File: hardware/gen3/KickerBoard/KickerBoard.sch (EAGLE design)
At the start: 87 parts, among them IC1 TL331, Q3 MOSFET-NCHANNELFQP30N06L, Q4 MOSFET-NCHANNELBSS123LT1G, Q6 MOSFET-PCHANNEL, U1 NC7WZ08K8X, U2 ATMEGA165PV-8AU

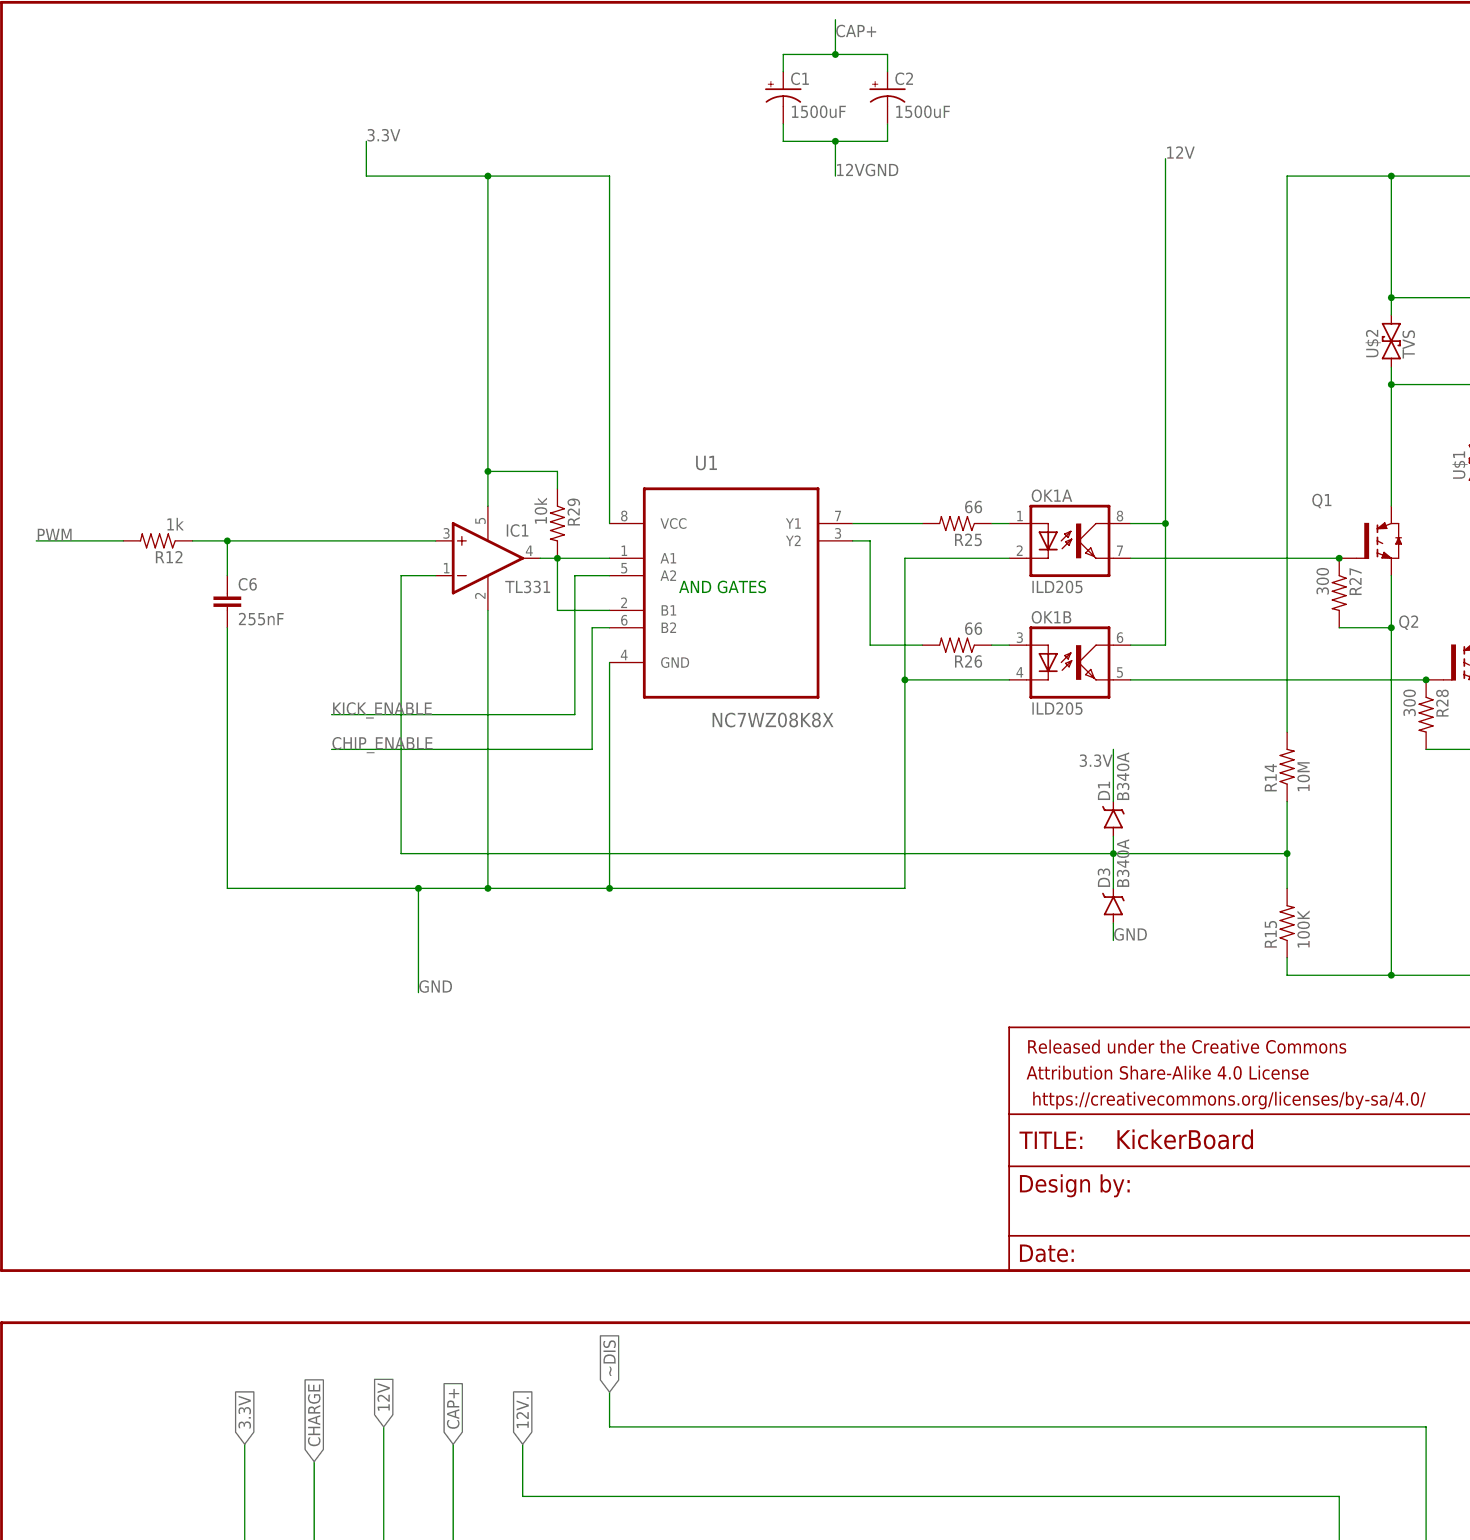
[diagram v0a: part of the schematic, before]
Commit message: reading in fault pins
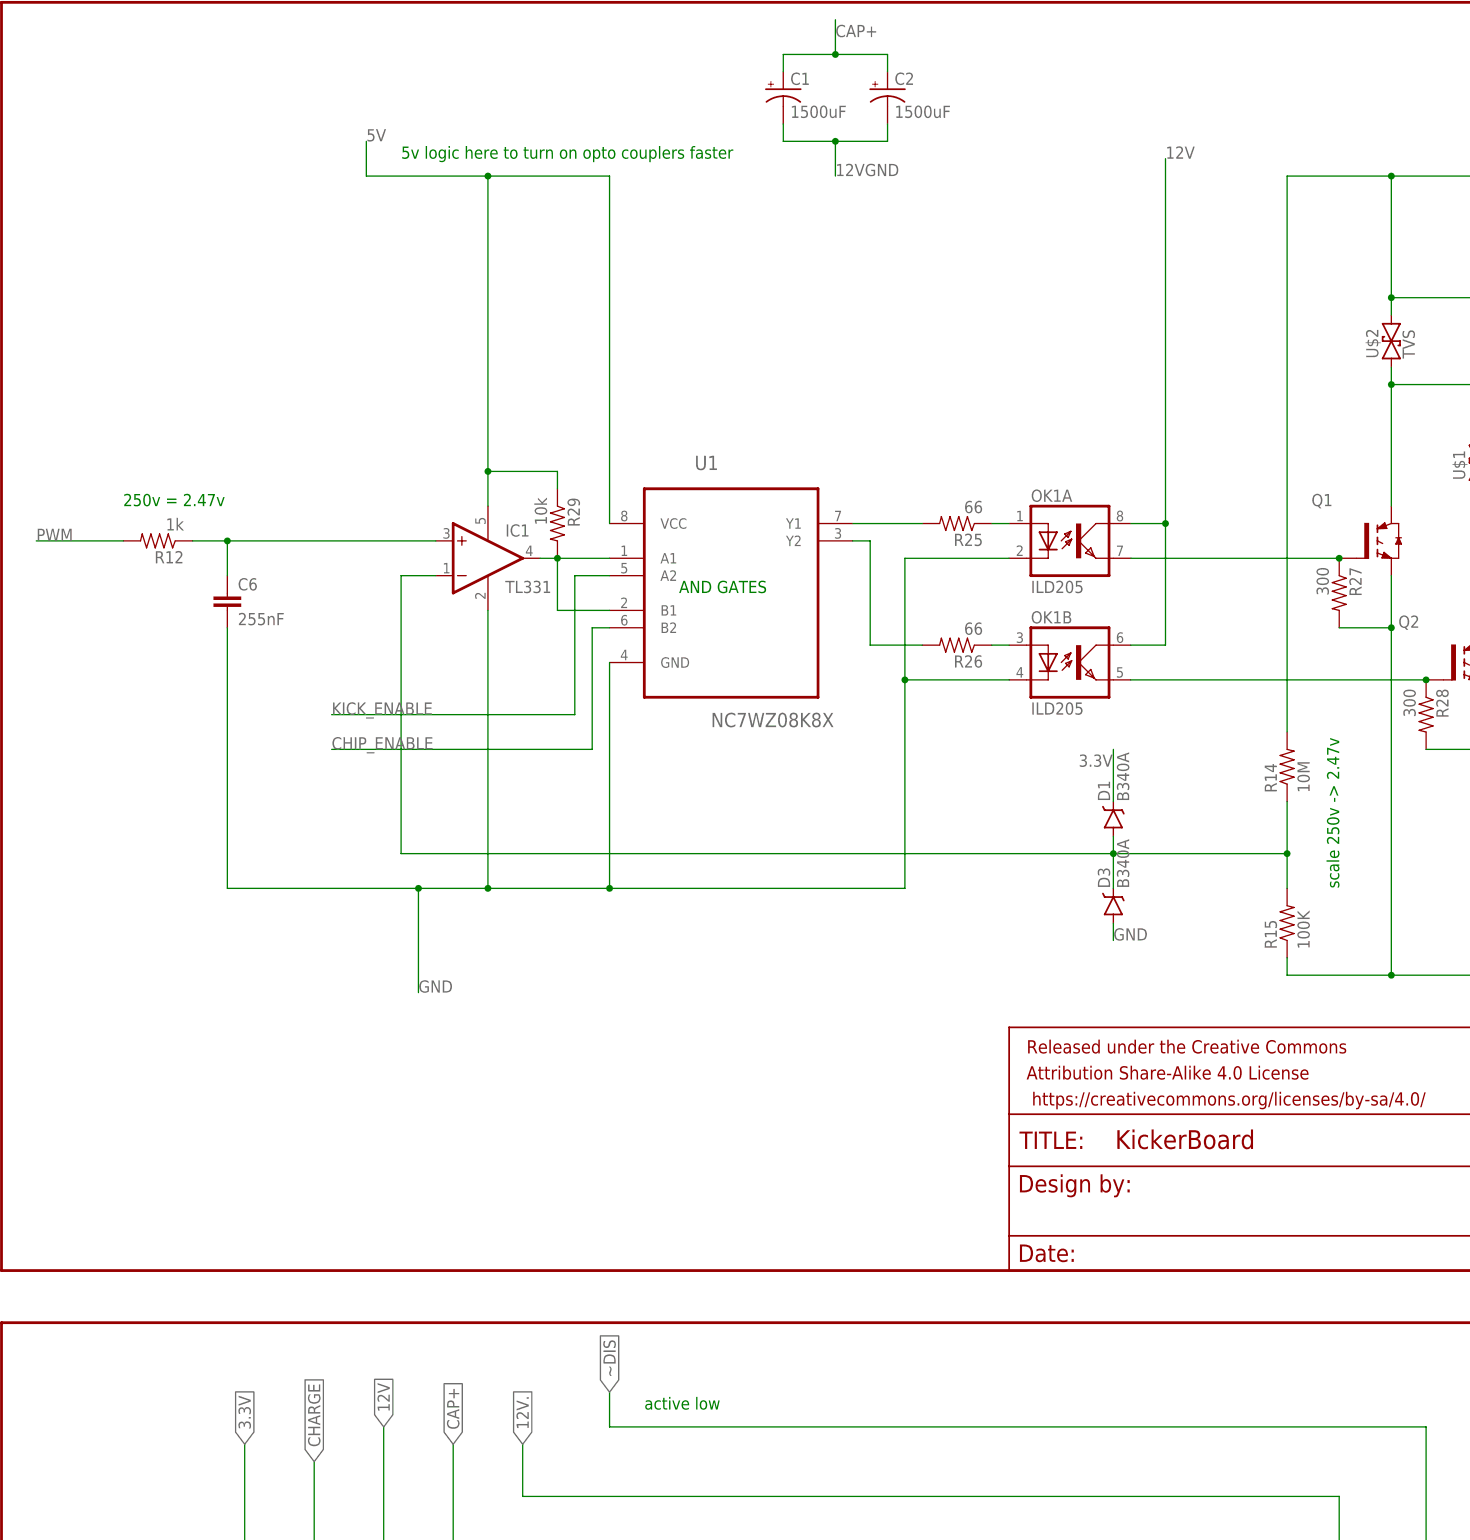
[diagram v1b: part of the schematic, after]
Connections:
- net 3.3V: no longer IC1.V+, R29.1, U1.VCC
- net 5V: now also IC1.V+, R29.1, U1.VCC
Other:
- note added: "250v = 2.47v"
- note added: "5v logic here to turn on opto couplers faster"
- note added: "active low"
- note added: "scale 250v -> 2.47v"
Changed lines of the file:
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@@
 <text x="160.02" y="241.3" size="1.778" layer="91">TODO: make sure works with 3.3v</text>
 <text x="459.74" y="91.44" size="1.778" layer="91">careful, this is pchannel</text>
+<text x="317.5" y="355.6" size="1.778" layer="91">5v logic here to turn on opto couplers faster</text>
+<text x="454.66" y="248.92" size="1.778" layer="91" rot="R90">scale 250v -&gt; 2.47v</text>
+<text x="276.86" y="304.8" size="1.778" layer="91">250v = 2.47v</text>
+<text x="353.06" y="172.72" size="1.778" layer="91">active low</text>
 </plain>
 <instances>
@@
 </segment>
 <segment>
-<pinref part="U1" gate="A" pin="VCC"/>
-<wire x1="347.98" y1="302.26" x2="347.98" y2="353.06" width="0.1524" layer="91"/>
-<wire x1="347.98" y1="353.06" x2="330.2" y2="353.06" width="0.1524" layer="91"/>
-<wire x1="330.2" y1="353.06" x2="312.42" y2="353.06" width="0.1524" layer="91"/>
-<wire x1="312.42" y1="353.06" x2="312.42" y2="358.14" width="0.1524" layer="91"/>
-<pinref part="IC1" gate="G$1" pin="V+"/>
-<wire x1="330.2" y1="304.8" x2="330.2" y2="309.88" width="0.1524" layer="91"/>
-<junction x="330.2" y="353.06"/>
-<label x="312.42" y="358.14" size="1.778" layer="95"/>
-<pinref part="R29" gate="G$1" pin="1"/>
-<wire x1="330.2" y1="309.88" x2="330.2" y2="353.06" width="0.1524" layer="91"/>
-<wire x1="340.36" y1="307.34" x2="340.36" y2="309.88" width="0.1524" layer="91"/>
-<wire x1="340.36" y1="309.88" x2="330.2" y2="309.88" width="0.1524" layer="91"/>
-<junction x="330.2" y="309.88"/>
-</segment>
-<segment>
 <pinref part="R7" gate="G$1" pin="1"/>
 <wire x1="294.64" y1="129.54" x2="294.64" y2="167.64" width="0.1524" layer="91"/>
@@
 <junction x="33.02" y="160.02"/>
 </segment>
-</net>
+<segment>
+<pinref part="U1" gate="A" pin="VCC"/>
+<wire x1="347.98" y1="302.26" x2="347.98" y2="353.06" width="0.1524" layer="91"/>
+<wire x1="347.98" y1="353.06" x2="330.2" y2="353.06" width="0.1524" layer="91"/>
+<wire x1="330.2" y1="353.06" x2="312.42" y2="353.06" width="0.1524" layer="91"/>
+<wire x1="312.42" y1="353.06" x2="312.42" y2="358.14" width="0.1524" layer="91"/>
+<pinref part="IC1" gate="G$1" pin="V+"/>
+<wire x1="330.2" y1="304.8" x2="330.2" y2="309.88" width="0.1524" layer="91"/>
+<junction x="330.2" y="353.06"/>
+<label x="312.42" y="358.14" size="1.778" layer="95"/>
+<pinref part="R29" gate="G$1" pin="1"/>
+<wire x1="330.2" y1="309.88" x2="330.2" y2="353.06" width="0.1524" layer="91"/>
+<wire x1="340.36" y1="307.34" x2="340.36" y2="309.88" width="0.1524" layer="91"/>
+<wire x1="340.36" y1="309.88" x2="330.2" y2="309.88" width="0.1524" layer="91"/>
+<junction x="330.2" y="309.88"/>
+</segment>
+</net>

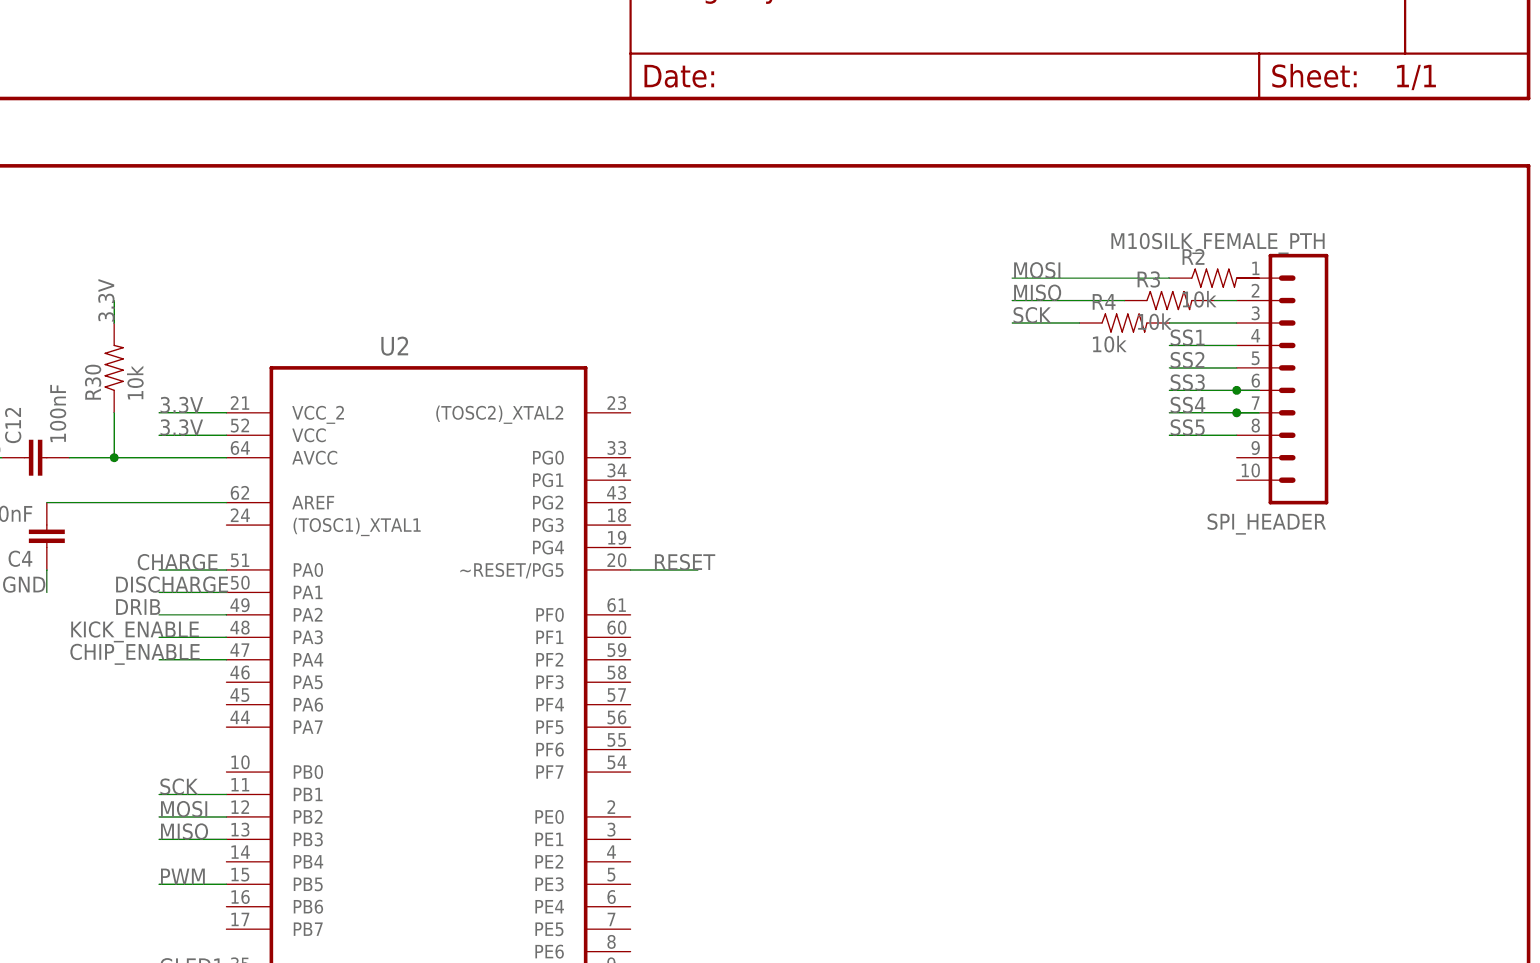
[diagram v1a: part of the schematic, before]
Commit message: hooked up ss lines
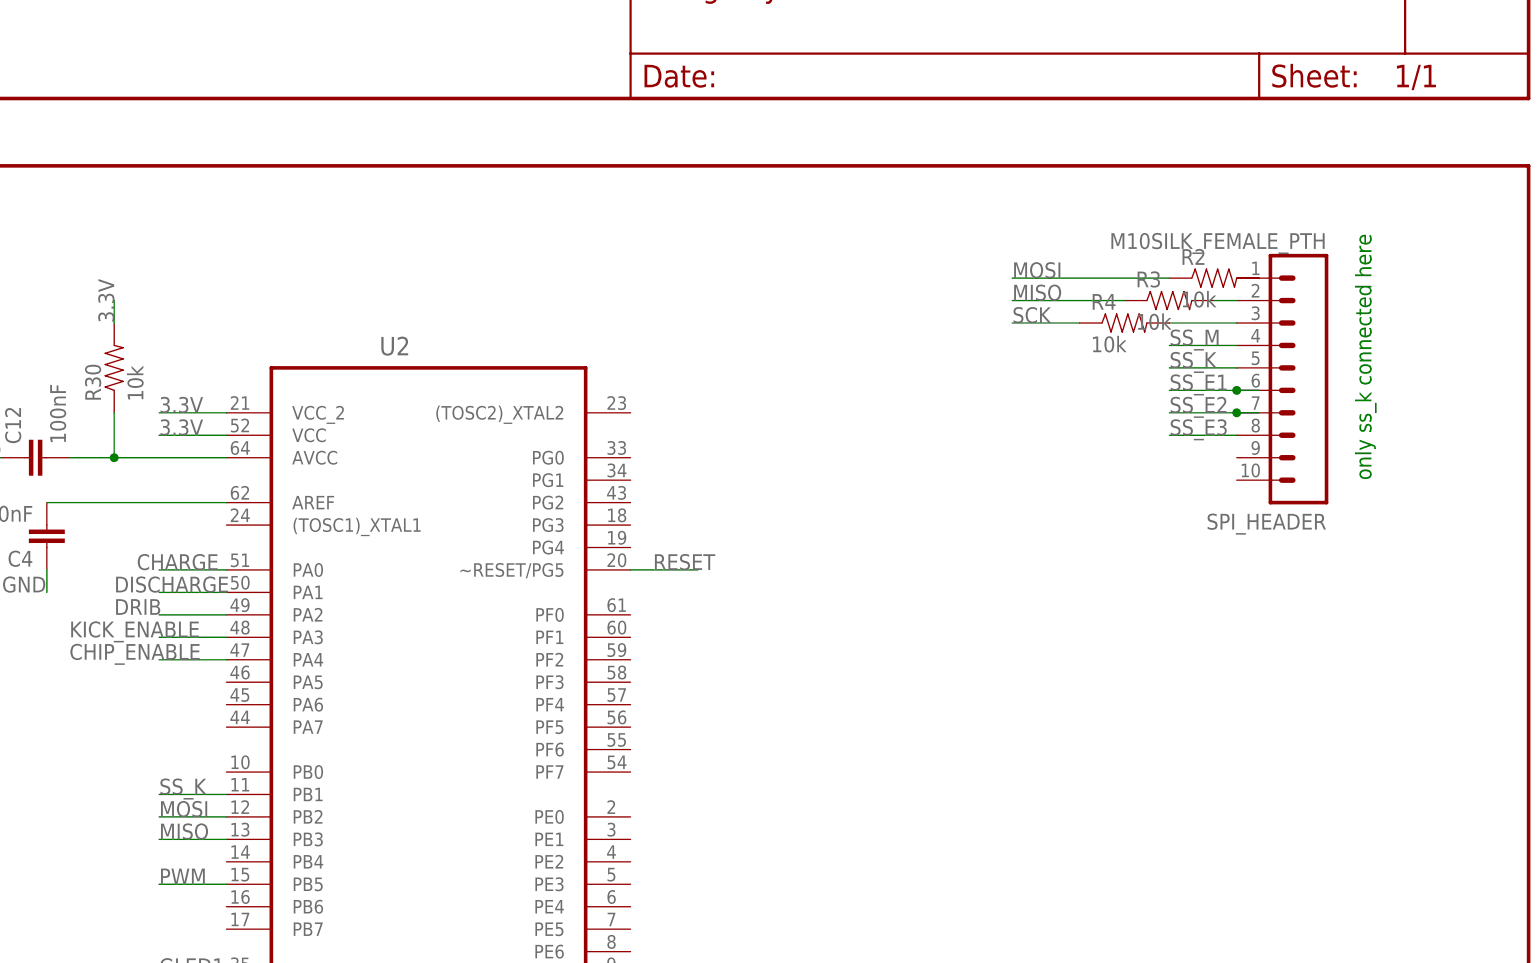
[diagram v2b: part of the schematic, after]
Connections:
- net SS1 renamed SS_M
- net SS3 renamed SS_E1
- net SS4 renamed SS_E2
- net SS5 renamed SS_E3
- removed net SS2: SPI_HEADER.5
- new net SS_K: SPI_HEADER.5, U2.PB1
- net SCK: no longer U2.PB1
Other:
- note added: "only ss_k connected here"
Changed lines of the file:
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@@
 <text x="276.86" y="304.8" size="1.778" layer="91">250v = 2.47v</text>
 <text x="353.06" y="172.72" size="1.778" layer="91">active low</text>
+<text x="231.14" y="149.86" size="1.778" layer="91" rot="R90">only ss_k connected here</text>
 </plain>
 <instances>
@@
 <label x="81.28" y="27.94" size="1.778" layer="95"/>
 </segment>
+</net>
+<net name="SS_M" class="0">
+<segment>
+<pinref part="SPI_HEADER" gate="G$1" pin="4"/>
+<wire x1="215.9" y1="165.1" x2="208.28" y2="165.1" width="0.1524" layer="91"/>
+<label x="208.28" y="165.1" size="1.778" layer="95"/>
+</segment>
+</net>
+<net name="SS_K" class="0">
+<segment>
+<pinref part="SPI_HEADER" gate="G$1" pin="5"/>
+<wire x1="215.9" y1="162.56" x2="208.28" y2="162.56" width="0.1524" layer="91"/>
+<label x="208.28" y="162.56" size="1.778" layer="95"/>
+</segment>
 <segment>
 <pinref part="U2" gate="A" pin="PB1"/>
@@
 </segment>
 </net>
-<net name="SS1" class="0">
-<segment>
-<pinref part="SPI_HEADER" gate="G$1" pin="4"/>
-<wire x1="215.9" y1="165.1" x2="208.28" y2="165.1" width="0.1524" layer="91"/>
-<label x="208.28" y="165.1" size="1.778" layer="95"/>
-</segment>
-</net>
-<net name="SS2" class="0">
-<segment>
-<pinref part="SPI_HEADER" gate="G$1" pin="5"/>
-<wire x1="215.9" y1="162.56" x2="208.28" y2="162.56" width="0.1524" layer="91"/>
-<label x="208.28" y="162.56" size="1.778" layer="95"/>
-</segment>
-</net>
-<net name="SS3" class="0">
+<net name="SS_E1" class="0">
 <segment>
 <wire x1="218.44" y1="160.02" x2="215.9" y2="160.02" width="0.1524" layer="91"/>
@@
 </segment>
 </net>
-<net name="SS4" class="0">
+<net name="SS_E2" class="0">
 <segment>
 <wire x1="218.44" y1="157.48" x2="215.9" y2="157.48" width="0.1524" layer="91"/>
@@
 </segment>
 </net>
-<net name="SS5" class="0">
+<net name="SS_E3" class="0">
 <segment>
 <pinref part="SPI_HEADER" gate="G$1" pin="8"/>

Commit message: fixed ERCs on all boards
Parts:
- removed C8100PF: (no value), rcl:C-EUC0805
- removed R10: (no value), resistor:R-US_R0805
- added C82: 100pF, rcl:C-EUC0805
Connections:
- removed net DISCHARGE: U2.PA1
- removed net N$20: BATT-2.KL
- new net DONE: R7.2, U$4.P$2, U2.PA5
- net 12VGND: now also BATT-2.KL, Q3.S, R9.1, U$3.P$10
- net CHARGE: no longer R10.1
- net GND: now also C82.2; no longer C8100PF.2, Q3.S, R10.2, R9.1, U$3.P$10
- net N$12: now also R2.2, SPI_HEADER.1; no longer R7.2, U$4.P$2
- net N$19: now also S1.P
- net N$6: now also C82.1; no longer C8100PF.1
- net ~DIS: now also U2.PA1
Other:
- moved on the sheet: R2
